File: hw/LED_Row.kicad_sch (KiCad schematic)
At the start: 3 parts, among them Q2 2N7002T, Q3 2N7002T, Q4 2N7002T

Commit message: updated Designs
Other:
- added sheet RGB LED Cell2_10 (RGB_LED_Cell2.kicad_sch)
- added sheet RGB LED Cell2_11 (RGB_LED_Cell2.kicad_sch)
- added sheet RGB LED Cell2_12 (RGB_LED_Cell2.kicad_sch)
- added sheet RGB LED Cell2_7 (RGB_LED_Cell2.kicad_sch)
- added sheet RGB LED Cell2_8 (RGB_LED_Cell2.kicad_sch)
- added sheet RGB LED Cell2_9 (RGB_LED_Cell2.kicad_sch)
- sheet RGB LED Cell2_1 ports: added VDD; removed none
- sheet RGB LED Cell2_2 ports: added VDD; removed none
- sheet RGB LED Cell2_3 ports: added VDD; removed none
- sheet RGB LED Cell2_4 ports: added VDD; removed none
- sheet RGB LED Cell2_5 ports: added VDD; removed none
- sheet RGB LED Cell2_6 ports: added VDD; removed none

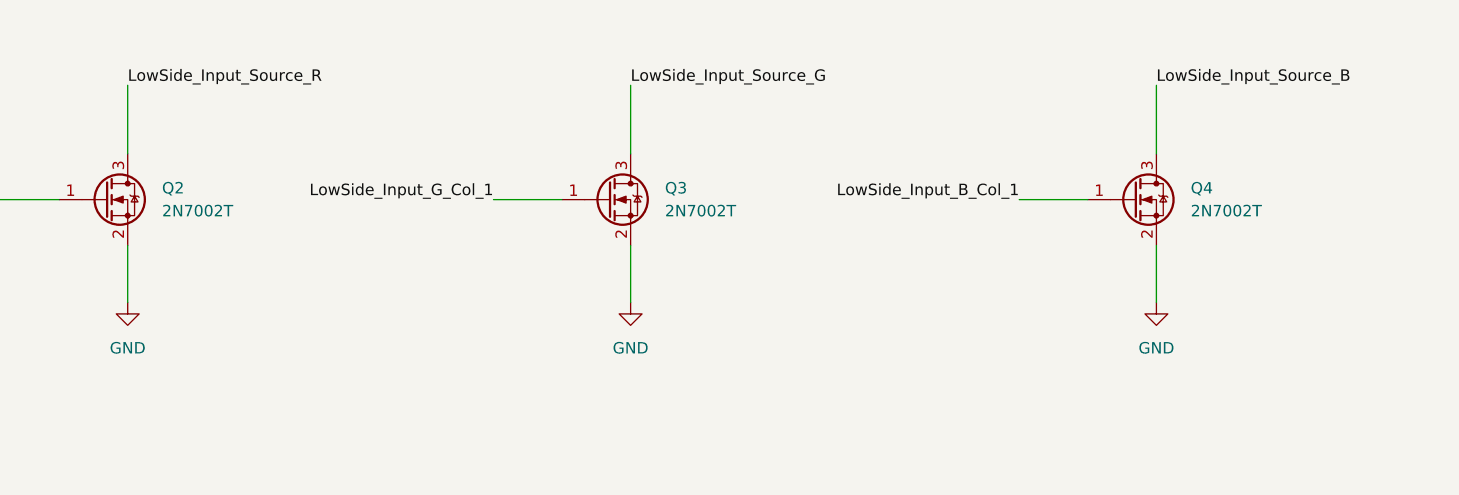
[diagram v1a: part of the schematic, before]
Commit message: replace all N-MOS components
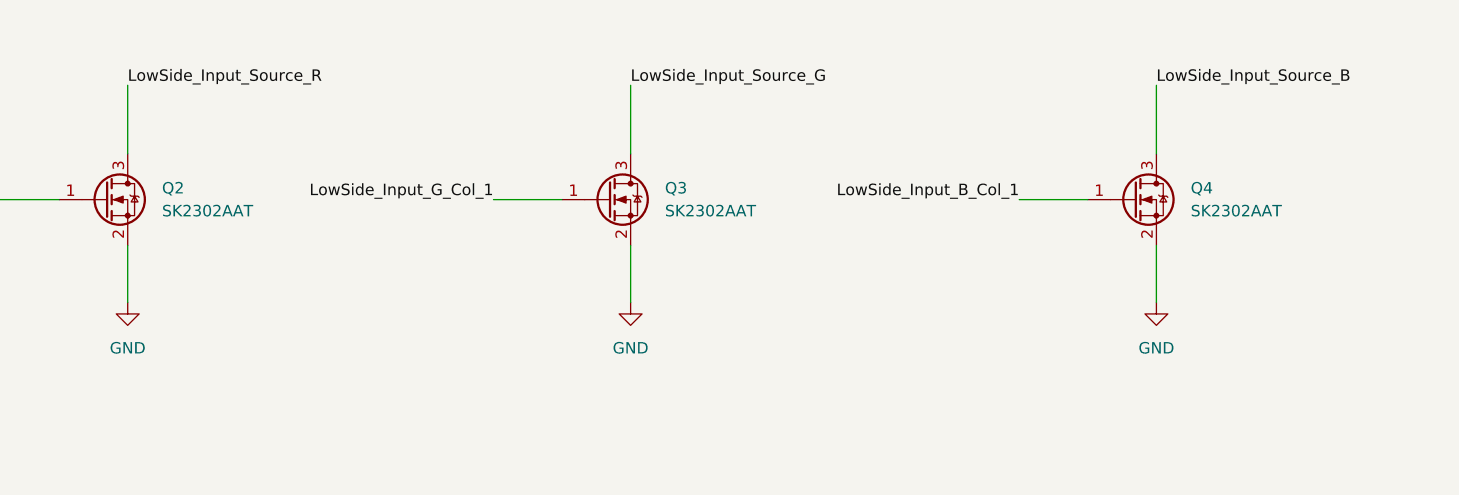
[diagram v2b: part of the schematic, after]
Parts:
- Q2, Q3, Q4: value 2N7002T -> SK2302AAT; LCSC C5224243 -> C475757; Vendor ElecSuper(静芯微） -> SHIKUES(时科); Vendor Model 2N7002T -> SK2302AAT
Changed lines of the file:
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@@
       (effects (font (size 1.27 1.27)) (justify left))
     )
-    (property "Value" "2N7002T" (at 243.84 36.83 0)
+    (property "Value" "SK2302AAT" (at 243.84 36.83 0)
       (effects (font (size 1.27 1.27)) (justify left))
     )
@@
       (effects (font (size 1.27 1.27)) hide)
     )
-    (property "Description" "类型: N沟道 漏源电压(Vdss): 60V 连续漏极电流(Id): 300mA 功率(Pd): 200mW 导通电阻(RDS(on)@Vgs,Id):" (at 237.49 35.56 0)
+    (property "Description" "类型：N沟道 漏源电压(Vdss)：20V 连续漏极电流(Id)：2.1A 功率(Pd)：350mW 导通电阻(RDS(on)@Vgs,Id)：60mΩ@4.5V,2A" (at 237.49 35.56 0)
       (effects (font (size 1.27 1.27)) hide)
     )
-    (property "LCSC" "C5224243" (at 237.49 35.56 0)
+    (property "LCSC" "C475757" (at 237.49 35.56 0)
       (effects (font (size 1.27 1.27)) hide)
     )
-    (property "Vendor" "ElecSuper(静芯微）" (at 237.49 35.56 0)
+    (property "Vendor" " SHIKUES(时科)" (at 237.49 35.56 0)
       (effects (font (size 1.27 1.27)) hide)
     )
-    (property "Vendor Model" "2N7002T" (at 237.49 35.56 0)
+    (property "Vendor Model" "SK2302AAT" (at 237.49 35.56 0)
       (effects (font (size 1.27 1.27)) hide)
     )
@@
       (effects (font (size 1.27 1.27)) (justify left))
     )
-    (property "Value" "2N7002T" (at 185.42 36.83 0)
+    (property "Value" "SK2302AAT" (at 185.42 36.83 0)
       (effects (font (size 1.27 1.27)) (justify left))
     )
@@
       (effects (font (size 1.27 1.27)) hide)
     )
-    (property "Description" "类型: N沟道 漏源电压(Vdss): 60V 连续漏极电流(Id): 300mA 功率(Pd): 200mW 导通电阻(RDS(on)@Vgs,Id):" (at 179.07 35.56 0)
+    (property "Description" "类型：N沟道 漏源电压(Vdss)：20V 连续漏极电流(Id)：2.1A 功率(Pd)：350mW 导通电阻(RDS(on)@Vgs,Id)：60mΩ@4.5V,2A" (at 179.07 35.56 0)
       (effects (font (size 1.27 1.27)) hide)
     )
-    (property "LCSC" "C5224243" (at 179.07 35.56 0)
+    (property "LCSC" "C475757" (at 179.07 35.56 0)
       (effects (font (size 1.27 1.27)) hide)
     )
-    (property "Vendor" "ElecSuper(静芯微）" (at 179.07 35.56 0)
+    (property "Vendor" " SHIKUES(时科)" (at 179.07 35.56 0)
       (effects (font (size 1.27 1.27)) hide)
     )
-    (property "Vendor Model" "2N7002T" (at 179.07 35.56 0)
+    (property "Vendor Model" "SK2302AAT" (at 179.07 35.56 0)
       (effects (font (size 1.27 1.27)) hide)
     )
@@
       (effects (font (size 1.27 1.27)) (justify left))
     )
-    (property "Value" "2N7002T" (at 129.54 36.83 0)
+    (property "Value" "SK2302AAT" (at 129.54 36.83 0)
       (effects (font (size 1.27 1.27)) (justify left))
     )
@@
       (effects (font (size 1.27 1.27)) hide)
     )
-    (property "Description" "类型: N沟道 漏源电压(Vdss): 60V 连续漏极电流(Id): 300mA 功率(Pd): 200mW 导通电阻(RDS(on)@Vgs,Id):" (at 123.19 35.56 0)
+    (property "Description" "类型：N沟道 漏源电压(Vdss)：20V 连续漏极电流(Id)：2.1A 功率(Pd)：350mW 导通电阻(RDS(on)@Vgs,Id)：60mΩ@4.5V,2A" (at 123.19 35.56 0)
       (effects (font (size 1.27 1.27)) hide)
     )
-    (property "LCSC" "C5224243" (at 123.19 35.56 0)
+    (property "LCSC" "C475757" (at 123.19 35.56 0)
       (effects (font (size 1.27 1.27)) hide)
     )
-    (property "Vendor" "ElecSuper(静芯微）" (at 123.19 35.56 0)
+    (property "Vendor" " SHIKUES(时科)" (at 123.19 35.56 0)
       (effects (font (size 1.27 1.27)) hide)
     )
-    (property "Vendor Model" "2N7002T" (at 123.19 35.56 0)
+    (property "Vendor Model" "SK2302AAT" (at 123.19 35.56 0)
       (effects (font (size 1.27 1.27)) hide)
     )
